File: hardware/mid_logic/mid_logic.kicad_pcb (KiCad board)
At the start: 2 copper layers, 52 x 52 mm, 28 parts, among them J2 J_STK_A, J3 J_STK_B, J4 RS485 A/B/GND, J5 EXP P6/P7, Q2 BC847, SW1 RESET, SW2 BOOT, U1 ESP32-S3-WROOM-1-N16R8, U2 MAX3485, U3 PCF8574

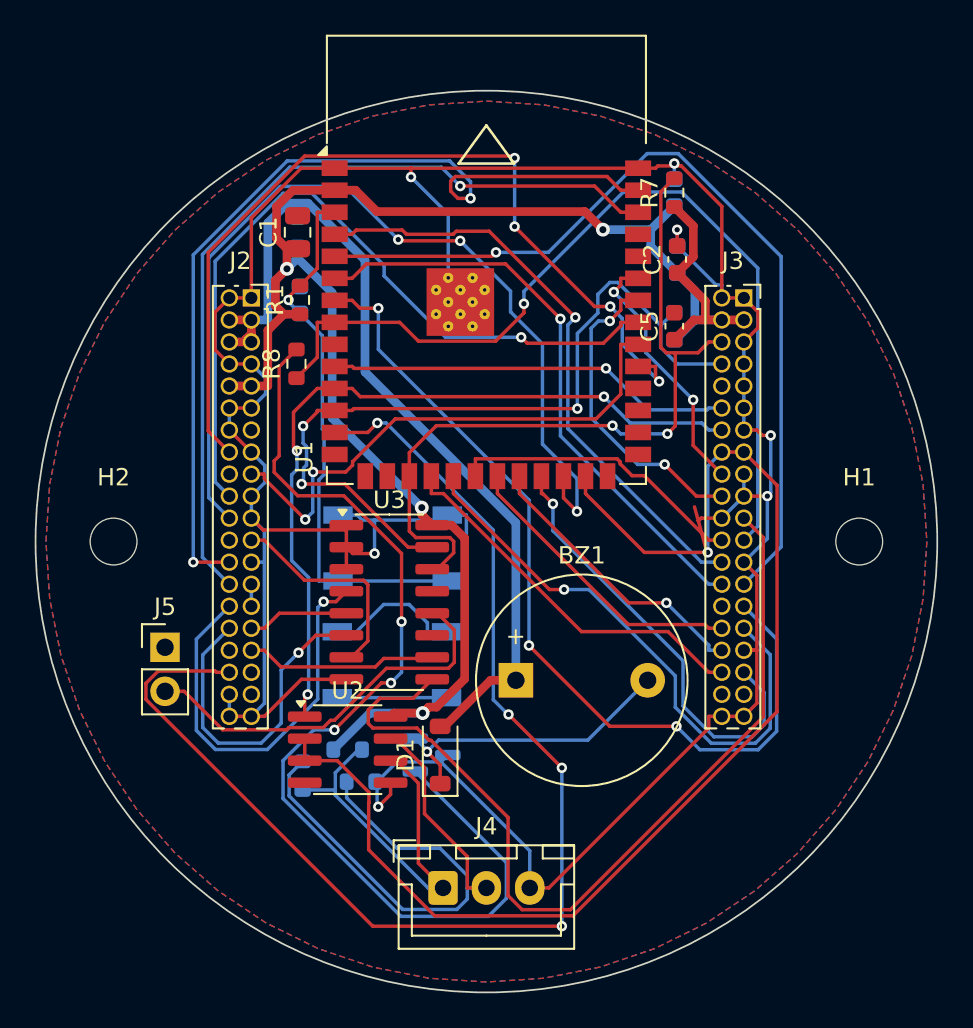
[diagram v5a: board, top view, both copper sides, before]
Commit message: Mid: frischer Komplett-Lauf - alle Signalnetze geroutet
Der Neustart von Null loeste die Oszillation: 655 Segmente, 73 Vias,
0 offene Signalverbindungen, Kupfer-DRC sauber. Offen sind nur noch
27 PGND-Paare (Pour-Erreichbarkeit nach dem dichteren Routing);
2 Stitching-Vias gesetzt, der PGND-als-Netz-Lauf laeuft.

Co-Authored-By: Claude Fable 5 <noreply@anthropic.com>
Claude-Session: https://claude.ai/code/session_017FTFDJW9R41k2WFeDRNE3w
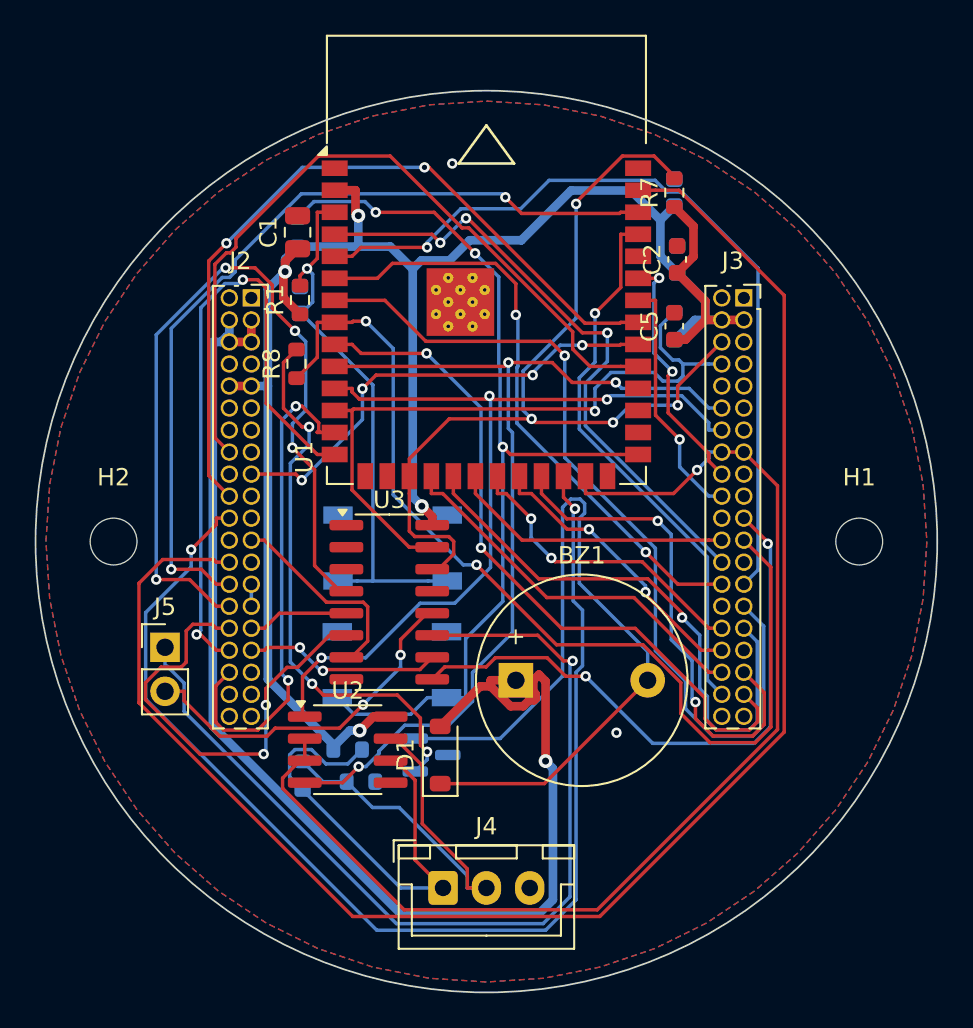
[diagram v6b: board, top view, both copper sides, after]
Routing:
- net PGND: track 214.6 -> 0.00 mm, vias 7 -> 2
- net EXP_P6: track 0.00 -> 54.6 mm, vias 0 -> 1
- net ESP_BOOT: track 6.30 -> 55.2 mm, vias 0 -> 3
- net I_SENSE1: track 52.6 -> 95.6 mm, vias 2 -> 0
- net USB_DN: track 71.9 -> 29.0 mm, vias 4 -> 2
- net DISP_RST: track 0.00 -> 41.1 mm, vias 0 -> 2
- net USB_DP: track 0.00 -> 37.7 mm, vias 0 -> 2
- net UART485_TX: track 23.4 -> 55.8 mm, vias 1 -> 3
- net DISP_BL: track 0.00 -> 31.9 mm, vias 0 -> 1
- net AUDIO_LOW: track 17.6 -> 47.7 mm, vias 1 -> 0
- net AUDIO_B: track 60.5 -> 32.0 mm
- net 5V_SYS: track 51.4 -> 75.4 mm, vias 0 -> 1
- net HW_TRIP1: track 23.9 -> 47.9 mm, vias 1 -> 4
- net RADAR_INT: track 51.6 -> 35.1 mm, vias 0 -> 2
- net M2_INB: track 53.8 -> 69.1 mm, vias 3 -> 2
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
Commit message: GND-Stitching: Segment-Freiraumpruefung, PTH-Regex, SMD-Fallback
seg_clear prueft geplante Stubs jetzt als Strecke gegen alles fremde
Kupfer der Lage (Segment-Segment-Distanz) statt nur den Endpunkt -
die 7 kollidierenden Blindstubs an den Steckerspalten sind entfernt.
Mid steht bei 12 offenen PGND-Paaren (Signale komplett, Kupfer-DRC
sauber); die Reste sind Steckerpins hinter Wand-Verticals und werden
zusammen mit dem Bottom-Ergebnis gezielt geschlossen.

Co-Authored-By: Claude Fable 5 <noreply@anthropic.com>
Claude-Session: https://claude.ai/code/session_017FTFDJW9R41k2WFeDRNE3w
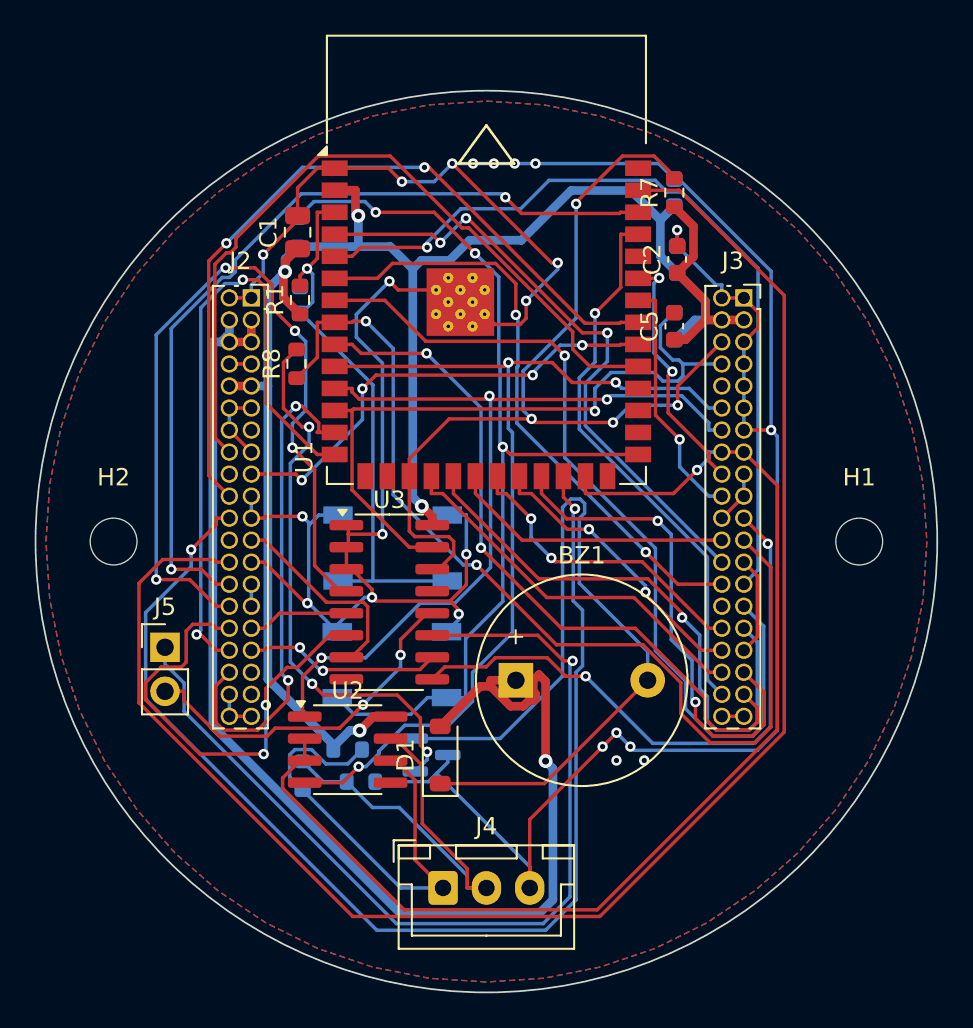
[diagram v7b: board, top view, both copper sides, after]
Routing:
- net PGND: track 0.00 -> 223.1 mm, vias 2 -> 23

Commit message: Fertigungsdaten Top + Stuecklisten; Routing-Stand dokumentiert
hardware/fab/top_ui.zip (Gerber, Excellon inkl. PDF-Karte, Positionen)
nach bestandenem DRC-Gate; BOMs fuer alle drei Boards aus den
Schaltplan-Generatoren. README-Status und docs/05 um den ehrlichen
Routing-Stand ergaenzt: Top vollstaendig; Mid 10 PGND-Pour-Anbindungen
offen (Push-and-Shove-Handgriff); Bottom ~85 %, Leistungsteil ist
laut Pruefliste ohnehin Handarbeit. gnd_connect.py (Union-Find-
Clusteranalyse) als Werkzeug ergaenzt.

Co-Authored-By: Claude Fable 5 <noreply@anthropic.com>
Claude-Session: https://claude.ai/code/session_017FTFDJW9R41k2WFeDRNE3w
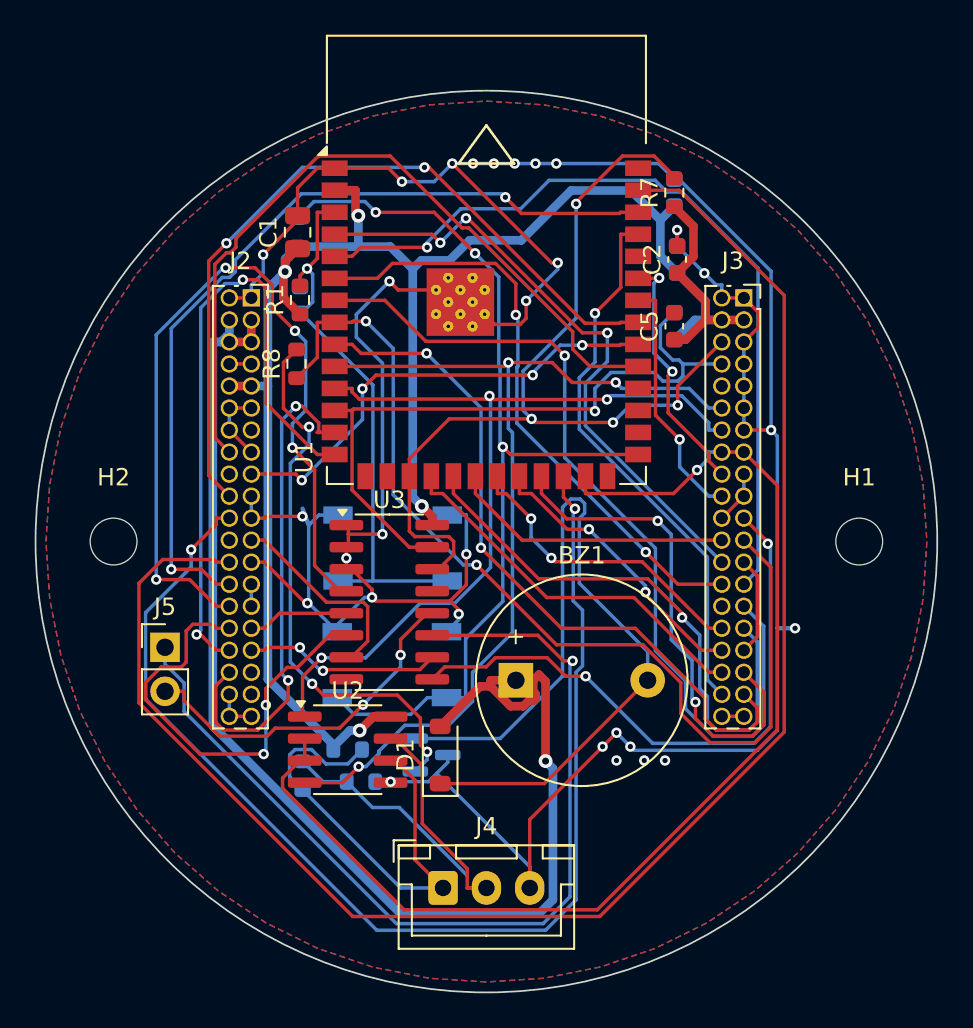
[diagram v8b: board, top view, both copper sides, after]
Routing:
- net PGND: track 223.1 -> 225.2 mm, vias 23 -> 29
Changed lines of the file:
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@@
   (segment (start -14.825 -10.24) (end -13.555 -10.24) (width 0.2) (layer "F.Cu") (net 30))
   (segment (start -7.9621 -0.4233) (end -5.9936 -0.4233) (width 0.2) (layer "F.Cu") (net 30))
+  (via (at 4.03019 -21.8) (size 0.6) (drill 0.3) (layers "F.Cu" "B.Cu") (net 30))
   (via (at 6.7012 11.825763) (size 0.6) (drill 0.3) (layers "F.Cu" "B.Cu") (net 30))
   (via (at 11 -17.9638) (size 0.6) (drill 0.3) (layers "F.Cu" "B.Cu") (net 30))
@@
   (via (at -1.597 4.1808) (size 0.6) (drill 0.3) (layers "F.Cu" "B.Cu") (net 30))
   (via (at 4.1141 -16.0756) (size 0.6) (drill 0.3) (layers "F.Cu" "B.Cu") (net 30))
+  (via (at -5.525 13.85) (size 0.6) (drill 0.3) (layers "F.Cu" "B.Cu") (net 30))
   (via (at -10.6073 -1.4506) (size 0.6) (drill 0.3) (layers "F.Cu" "B.Cu") (net 30))
+  (via (at 12.57017 -15.47483) (size 0.6) (drill 0.3) (layers "F.Cu" "B.Cu") (net 30))
+  (via (at -8.074999 0.96) (size 0.6) (drill 0.3) (layers "F.Cu" "B.Cu") (net 30))
   (via (at -0.76981 -21.8) (size 0.6) (drill 0.3) (layers "F.Cu" "B.Cu") (net 30))
   (via (at 0.43019 -21.8) (size 0.6) (drill 0.3) (layers "F.Cu" "B.Cu") (net 30))
   (via (at 8.3012 11.825763) (size 0.6) (drill 0.3) (layers "F.Cu" "B.Cu") (net 30))
+  (via (at 17.8 5) (size 0.6) (drill 0.3) (layers "F.Cu" "B.Cu") (net 30))
   (via (at 2.83019 -21.8) (size 0.6) (drill 0.3) (layers "F.Cu" "B.Cu") (net 30))
+  (via (at 10.3012 12.625763) (size 0.6) (drill 0.3) (layers "F.Cu" "B.Cu") (net 30))
   (via (at 1.63019 -21.8) (size 0.6) (drill 0.3) (layers "F.Cu" "B.Cu") (net 30))
   (via (at -1.1559 0.7318) (size 0.6) (drill 0.3) (layers "F.Cu" "B.Cu") (net 30))
@@
   (segment (start 8.5132 12.0378) (end 15.6279 12.0378) (width 0.2) (layer "B.Cu") (net 30))
   (segment (start 7.5012 11.0258) (end 8.5132 12.0378) (width 0.2) (layer "B.Cu") (net 30))
+  (segment (start -10.25 -0.94) (end -10.6 -1.9) (width 0.25) (layer "B.Cu") (net 30))
   (segment (start -10.2481 -0.9381) (end -10.1714 -1.0148) (width 0.2) (layer "B.Cu") (net 30))
   (segment (start -2.2278 12.3103) (end -2.2278 12.7331) (width 0.2) (layer "B.Cu") (net 30))
@@
   (segment (start 2.5 18.7481) (end -2.8714 13.3767) (width 0.2) (layer "B.Cu") (net 30))
   (segment (start -1.9698 -21.8) (end -3.014 -20.7558) (width 0.2) (layer "B.Cu") (net 30))
+  (segment (start 16.78 5) (end 17.8 5) (width 0.25) (layer "B.Cu") (net 30))
   (segment (start 13.2431 -14.8019) (end 13.575 -14.8019) (width 0.2) (layer "B.Cu") (net 30))
   (segment (start -1.597 4.5002) (end -2.2998 5.203) (width 0.2) (layer "B.Cu") (net 30))
@@
   (segment (start -15.0763 -14.8794) (end -14.2663 -14.8794) (width 0.2) (layer "B.Cu") (net 51))
   (zone (net 30) (net_name "PGND") (layer "F.Cu") (hatch edge 0.5)
-    (connect_pads (clearance 0.3))
+    (connect_pads yes (clearance 0.15))
     (min_thickness 0.25) (filled_areas_thickness no)
     (fill yes (thermal_gap 0.5) (thermal_bridge_width 0.5) (island_removal_mode 2) (island_area_min 4))
@@
   )
   (zone (net 30) (net_name "PGND") (layer "B.Cu") (hatch edge 0.5)
-    (connect_pads (clearance 0.3))
+    (connect_pads yes (clearance 0.15))
     (min_thickness 0.25) (filled_areas_thickness no)
     (fill yes (thermal_gap 0.5) (thermal_bridge_width 0.5) (island_removal_mode 2) (island_area_min 4))
